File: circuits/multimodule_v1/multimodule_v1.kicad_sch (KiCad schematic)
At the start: 1 part, among them U1 ESP32-WROOM-32

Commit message: Initial Schematic
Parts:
- added C1: 1uF, symbol Device:C
- added C2, C3, C4, C5, C6: 100nF, symbol Device:C
- added C7: 100uF, symbol Device:C_Polarized
- added D1, D2: LED, symbol Device:LED
- added J1: Light, symbol Connector:Conn_01x04_Socket
- added J2: Temp/Hump, symbol Connector:Conn_01x04_Socket
- added J3: LCDA, symbol Connector:Conn_01x04_Socket
- added J4: USB_B_Micro, symbol Connector:USB_B_Micro
- added J5: UART, symbol Connector:Conn_01x04_Socket
- added J6: BATT, symbol Connector:Conn_01x02_Socket
- added J7: CO2, symbol Connector:Conn_01x03_Socket
- added R1, R6: 0, symbol Device:R
- added R10: 100, symbol Device:R
- added R2, R3: 220, symbol Device:R
- added R4, R5: R, symbol Device:R
- added R7, R8: 10K, symbol Device:R
- added R9: 330, symbol Device:R
- added SW1, SW2: SW_Push, symbol Switch:SW_Push
- added U2: INMP441, symbol INMP441:INMP441
- added U3: CH340C, Package_SO:SOIC-16_3.9x9.9mm_P1.27mm, symbol Interface_USB:CH340C
- added U4: AMS1117-3.3, Package_TO_SOT_SMD:SOT-223-3_TabPin2, symbol Regulator_Linear:AMS1117-3.3
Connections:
- net GND: now also C1.2, C2.2, C3.2, C4.2, C5.2, C6.1, C7.2, D1.1 (K), J1.2 (Pin_2), J2.2 (Pin_2), J3.2 (Pin_2), J4.5 (GND), J4.6 (Shield), J5.2 (Pin_2), J6.1 (Pin_1), J7.2 (Pin_2), R1.2, R10.2, R6.2, SW1.1, SW2.1, U2.1 (GND), U3.1 (GND), U4.1 (GND)
- net VDD: now also C1.1, C2.1, C3.1, C6.2, J1.1 (Pin_1), J2.1 (Pin_1), J3.1 (Pin_1), J5.1 (Pin_1), R2.1, R3.1, R4.1, R5.1, R7.1, R8.1, U2.2 (VDD), U3.16 (VCC), U3.4 (V3), U4.2 (VO)
- net MIC_SCK: now reaches U1.13 (IO14)
- net MIC_SCK: now also U2.4 (BCLK)
- net MIC_WS: now reaches U1.16 (IO13)
- net MIC_WS: now also U2.5 (WS)
- net at U1.23 (IO15): now also R1.1
- net LED: now reaches U1.24 (IO2)
- net LED: now also D2.1 (K)
- net PROG: now reaches U1.25 (IO0)
- net PROG: now also C5.1, R5.2, SW2.2
- net RST: now reaches U1.3 (EN)
- net RST: now also C4.1, R4.2, SW1.2
- net I2C_SDA: now reaches U1.33 (IO21)
- net I2C_SDA: now also J1.3 (Pin_3), J2.3 (Pin_3), J3.3 (Pin_3), R7.2
- net RX0: now reaches U1.34 (RXD0/IO3)
- net RX0: now also J5.3 (Pin_3), U3.2 (TXD)
- net TX0: now reaches U1.35 (TXD0/IO1)
- net TX0: now also J5.4 (Pin_4), U3.3 (RXD)
- net I2C_SCL: now reaches U1.36 (IO22)
- net I2C_SCL: now also J1.4 (Pin_4), J2.4 (Pin_4), J3.4 (Pin_4), R8.2
- net MIC_DATA: now reaches U1.37 (IO23)
- net MIC_DATA: now also U2.3 (DATA)
- net CO2: now reaches U1.6 (IO34)
- net CO2: now also J7.3 (Pin_3)
- net VBAT: now reaches U1.9 (IO33)
- net VBAT: now also R10.1, R9.2
- new net: D1.2 (A), R2.2
- new net: D2.2 (A), R3.2
- new net: J4.2 (D-), U3.6 (UD-)
- new net: J4.3 (D+), U3.5 (UD+)
- new net: R6.1, U2.6 (LRC)
- new net VCC: C7.1, J6.2 (Pin_2), J7.1 (Pin_1), R9.1, U4.3 (VI)
- no-connect marks 0 -> 28
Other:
- note added: "ESP32 MCU"
- note added: "INPUTS"
- note added: "MIC INMP441"
- note added: "USB-UART"
- note added: "VREG"
- title: (none) -> Smarthome Monitoring Multimodule Prototype
- moved on the sheet: U1

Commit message: Initial Footprint
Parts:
- C1, C2, C3, C4, C5, C6: footprint (none) -> Capacitor_SMD:C_0805_2012Metric_Pad1.18x1.45mm_HandSolder
- C7: footprint (none) -> Capacitor_SMD:CP_Elec_4x5.8
- D1, D2: footprint (none) -> LED_SMD:LED_0805_2012Metric_Pad1.15x1.40mm_HandSolder
- J1, J2, J3: footprint (none) -> Connector_PinSocket_2.54mm:PinSocket_1x04_P2.54mm_Vertical
- J4: footprint (none) -> Connector_USB:USB_Micro-B_Wuerth_629105150521
- J5: footprint (none) -> Connector_PinHeader_2.54mm:PinHeader_1x04_P2.54mm_Vertical
- J6: footprint (none) -> TerminalBlock:TerminalBlock_Altech_AK300-2_P5.00mm
- J7: footprint (none) -> Connector_PinHeader_2.54mm:PinHeader_1x03_P2.54mm_Vertical
- R1, R10, R2, R3, R4, R5, R6, R7, R8, R9: footprint (none) -> Resistor_SMD:R_0805_2012Metric_Pad1.20x1.40mm_HandSolder
- SW1, SW2: footprint (none) -> Button_Switch_THT:SW_PUSH_6mm
- U2: footprint (none) -> INMP441:INMP441
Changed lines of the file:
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@@
       (effects (font (size 1.27 1.27)) (justify right) hide)
     )
-    (property "Footprint" "" (at 161.29 102.87 0)
+    (property "Footprint" "Button_Switch_THT:SW_PUSH_6mm" (at 161.29 102.87 0)
       (effects (font (size 1.27 1.27)) hide)
     )
@@
       (effects (font (size 1.27 1.27)) (justify left))
     )
-    (property "Footprint" "" (at 149.5552 135.89 0)
+    (property "Footprint" "Capacitor_SMD:CP_Elec_4x5.8" (at 149.5552 135.89 0)
       (effects (font (size 1.27 1.27)) hide)
     )
@@
       (effects (font (size 1.27 1.27)) (justify right) hide)
     )
-    (property "Footprint" "" (at 135.89 60.96 0)
+    (property "Footprint" "LED_SMD:LED_0805_2012Metric_Pad1.15x1.40mm_HandSolder" (at 135.89 60.96 0)
       (effects (font (size 1.27 1.27)) hide)
     )
@@
       (effects (font (size 1.27 1.27)) (justify left))
     )
-    (property "Footprint" "" (at 210.312 92.71 90)
+    (property "Footprint" "Resistor_SMD:R_0805_2012Metric_Pad1.20x1.40mm_HandSolder" (at 210.312 92.71 90)
       (effects (font (size 1.27 1.27)) hide)
     )
@@
       (effects (font (size 1.27 1.27)) (justify left))
     )
-    (property "Footprint" "" (at 131.7752 93.98 0)
+    (property "Footprint" "Capacitor_SMD:C_0805_2012Metric_Pad1.18x1.45mm_HandSolder" (at 131.7752 93.98 0)
       (effects (font (size 1.27 1.27)) hide)
     )
@@
       (effects (font (size 1.27 1.27)) (justify right) hide)
     )
-    (property "Footprint" "" (at 144.78 60.96 0)
+    (property "Footprint" "LED_SMD:LED_0805_2012Metric_Pad1.15x1.40mm_HandSolder" (at 144.78 60.96 0)
       (effects (font (size 1.27 1.27)) hide)
     )
@@
       (effects (font (size 1.27 1.27)))
     )
-    (property "Footprint" "" (at 87.63 144.78 0)
+    (property "Footprint" "Connector_USB:USB_Micro-B_Wuerth_629105150521" (at 87.63 144.78 0)
       (effects (font (size 1.27 1.27)) hide)
     )
@@
       (effects (font (size 1.27 1.27)) (justify left))
     )
-    (property "Footprint" "" (at 184.912 92.71 90)
+    (property "Footprint" "Resistor_SMD:R_0805_2012Metric_Pad1.20x1.40mm_HandSolder" (at 184.912 92.71 90)
       (effects (font (size 1.27 1.27)) hide)
     )
@@
       (effects (font (size 1.27 1.27)) (justify left))
     )
-    (property "Footprint" "" (at 164.592 92.71 90)
+    (property "Footprint" "Resistor_SMD:R_0805_2012Metric_Pad1.20x1.40mm_HandSolder" (at 164.592 92.71 90)
       (effects (font (size 1.27 1.27)) hide)
     )
@@
       (effects (font (size 1.27 1.27)))
     )
-    (property "Footprint" "" (at 193.04 64.77 0)
+    (property "Footprint" "Connector_PinSocket_2.54mm:PinSocket_1x04_P2.54mm_Vertical" (at 193.04 64.77 0)
       (effects (font (size 1.27 1.27)) hide)
     )
@@
       (effects (font (size 1.27 1.27)) (justify left))
     )
-    (property "Footprint" "" (at 171.1452 105.41 0)
+    (property "Footprint" "Capacitor_SMD:C_0805_2012Metric_Pad1.18x1.45mm_HandSolder" (at 171.1452 105.41 0)
       (effects (font (size 1.27 1.27)) hide)
     )
@@
       (effects (font (size 1.27 1.27)) (justify left))
     )
-    (property "Footprint" "" (at 156.972 132.08 90)
+    (property "Footprint" "Resistor_SMD:R_0805_2012Metric_Pad1.20x1.40mm_HandSolder" (at 156.972 132.08 90)
       (effects (font (size 1.27 1.27)) hide)
     )
@@
       (effects (font (size 1.27 1.27)))
     )
-    (property "Footprint" "" (at 102.87 128.5748 0)
+    (property "Footprint" "Capacitor_SMD:C_0805_2012Metric_Pad1.18x1.45mm_HandSolder" (at 102.87 128.5748 0)
       (effects (font (size 1.27 1.27)) hide)
     )
@@
       (effects (font (size 1.27 1.27)) (justify left))
     )
-    (property "Footprint" "" (at 172.4152 45.72 0)
+    (property "Footprint" "Capacitor_SMD:C_0805_2012Metric_Pad1.18x1.45mm_HandSolder" (at 172.4152 45.72 0)
       (effects (font (size 1.27 1.27)) hide)
     )
@@
       (effects (font (size 1.27 1.27)) (justify left))
     )
-    (property "Footprint" "" (at 143.002 53.34 90)
+    (property "Footprint" "Resistor_SMD:R_0805_2012Metric_Pad1.20x1.40mm_HandSolder" (at 143.002 53.34 90)
       (effects (font (size 1.27 1.27)) hide)
     )
@@
       (effects (font (size 1.27 1.27)))
     )
-    (property "Footprint" "" (at 165.1 64.77 0)
+    (property "Footprint" "Connector_PinSocket_2.54mm:PinSocket_1x04_P2.54mm_Vertical" (at 165.1 64.77 0)
       (effects (font (size 1.27 1.27)) hide)
     )
@@
       (effects (font (size 1.27 1.27)) (justify left))
     )
-    (property "Footprint" "" (at 156.972 140.97 90)
+    (property "Footprint" "Resistor_SMD:R_0805_2012Metric_Pad1.20x1.40mm_HandSolder" (at 156.972 140.97 90)
       (effects (font (size 1.27 1.27)) hide)
     )
@@
       (effects (font (size 1.27 1.27)))
     )
-    (property "Footprint" "" (at 207.01 64.77 0)
+    (property "Footprint" "Connector_PinHeader_2.54mm:PinHeader_1x03_P2.54mm_Vertical" (at 207.01 64.77 0)
       (effects (font (size 1.27 1.27)) hide)
     )
@@
       (effects (font (size 1.27 1.27)) (justify right) hide)
     )
-    (property "Footprint" "" (at 181.61 102.87 0)
+    (property "Footprint" "Button_Switch_THT:SW_PUSH_6mm" (at 181.61 102.87 0)
       (effects (font (size 1.27 1.27)) hide)
     )
@@
       (effects (font (size 1.27 1.27)))
     )
-    (property "Footprint" "" (at 179.07 64.77 0)
+    (property "Footprint" "Connector_PinSocket_2.54mm:PinSocket_1x04_P2.54mm_Vertical" (at 179.07 64.77 0)
       (effects (font (size 1.27 1.27)) hide)
     )
@@
       (effects (font (size 1.27 1.27)))
     )
-    (property "Footprint" "" (at 208.28 39.878 90)
+    (property "Footprint" "Resistor_SMD:R_0805_2012Metric_Pad1.20x1.40mm_HandSolder" (at 208.28 39.878 90)
       (effects (font (size 1.27 1.27)) hide)
     )
@@
       (effects (font (size 1.27 1.27)))
     )
-    (property "Footprint" "" (at 115.57 129.54 0)
+    (property "Footprint" "Connector_PinHeader_2.54mm:PinHeader_1x04_P2.54mm_Vertical" (at 115.57 129.54 0)
       (effects (font (size 1.27 1.27)) hide)
     )
@@
       (effects (font (size 1.27 1.27)))
     )
-    (property "Footprint" "" (at 118.11 66.548 90)
+    (property "Footprint" "Resistor_SMD:R_0805_2012Metric_Pad1.20x1.40mm_HandSolder" (at 118.11 66.548 90)
       (effects (font (size 1.27 1.27)) hide)
     )
@@
       (effects (font (size 1.27 1.27)) (justify left))
     )
-    (property "Footprint" "" (at 203.962 92.71 90)
+    (property "Footprint" "Resistor_SMD:R_0805_2012Metric_Pad1.20x1.40mm_HandSolder" (at 203.962 92.71 90)
       (effects (font (size 1.27 1.27)) hide)
     )
@@
       (effects (font (size 1.27 1.27)))
     )
-    (property "Footprint" "" (at 195.58 34.29 0)
+    (property "Footprint" "INMP441:INMP441" (at 195.58 34.29 0)
       (effects (font (size 1.27 1.27)) hide)
     )
@@
       (effects (font (size 1.27 1.27)) (justify left))
     )
-    (property "Footprint" "" (at 191.4652 105.41 0)
+    (property "Footprint" "Capacitor_SMD:C_0805_2012Metric_Pad1.18x1.45mm_HandSolder" (at 191.4652 105.41 0)
       (effects (font (size 1.27 1.27)) hide)
     )
@@
       (effects (font (size 1.27 1.27)) (justify left))
     )
-    (property "Footprint" "" (at 134.112 53.34 90)
+    (property "Footprint" "Resistor_SMD:R_0805_2012Metric_Pad1.20x1.40mm_HandSolder" (at 134.112 53.34 90)
       (effects (font (size 1.27 1.27)) hide)
     )
@@
       (effects (font (size 1.27 1.27)) (justify left))
     )
-    (property "Footprint" "" (at 143.2052 93.98 0)
+    (property "Footprint" "Capacitor_SMD:C_0805_2012Metric_Pad1.18x1.45mm_HandSolder" (at 143.2052 93.98 0)
       (effects (font (size 1.27 1.27)) hide)
     )
@@
       (effects (font (size 1.27 1.27)))
     )
-    (property "Footprint" "" (at 138.43 130.81 0)
-      (effects (font (size 1.27 1.27)) hide)
-    )
+    (property "Footprint" "TerminalBlock:TerminalBlock_Altech_AK300-2_P5.00mm" (at 138.43 130.81 0)
+      (effects (font (size 1.27 1.27)) hide)
+    )

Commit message: Update Custom module
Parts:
- J6: footprint TerminalBlock:TerminalBlock_Altech_AK300-2_P5.00mm -> TerminalBlock_4Ucon:TerminalBlock_4Ucon_1x02_P3.50mm_Horizontal
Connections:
- no-connect marks 28 -> 29
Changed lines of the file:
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@@
   (no_connect (at 115.57 148.59))
   (no_connect (at 91.44 138.43))
+  (no_connect (at 95.25 138.43))
   (no_connect (at 114.3 57.15))
   (no_connect (at 115.57 151.13))
@@
       (effects (font (size 1.27 1.27)))
     )
-    (property "Footprint" "TerminalBlock:TerminalBlock_Altech_AK300-2_P5.00mm" (at 138.43 130.81 0)
-      (effects (font (size 1.27 1.27)) hide)
-    )
+    (property "Footprint" "TerminalBlock_4Ucon:TerminalBlock_4Ucon_1x02_P3.50mm_Horizontal" (at 138.43 130.81 0)
+      (effects (font (size 1.27 1.27)) hide)
+    )

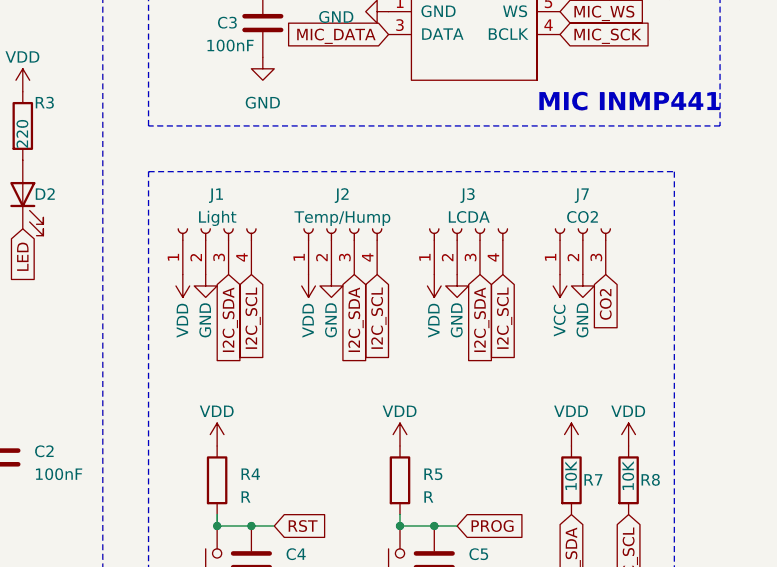
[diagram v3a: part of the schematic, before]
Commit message: Small PCB version
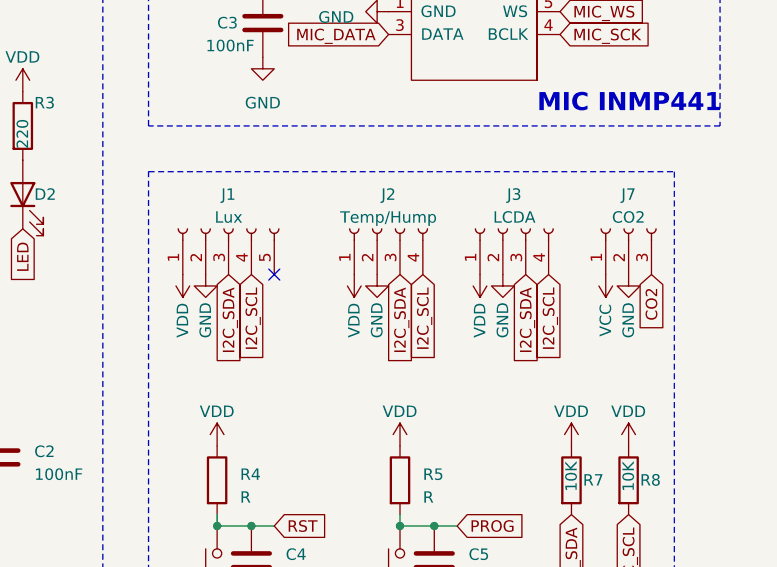
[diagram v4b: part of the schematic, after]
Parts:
- removed J1: Light, Connector_PinSocket_2.54mm:PinSocket_1x04_P2.54mm_Vertical, symbol Connector:Conn_01x04_Socket
- added J1: Lux, Connector_PinSocket_2.54mm:PinSocket_1x05_P2.54mm_Vertical, symbol Connector:Conn_01x05_Socket
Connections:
- net GND: now also J1.2 (Pin_2)
- net I2C_SCL: now also J1.4 (Pin_4)
- net I2C_SDA: now also J1.3 (Pin_3)
- net VDD: now also J1.1 (Pin_1)
- no-connect marks 29 -> 30
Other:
- moved on the sheet: J2, J3, J7
